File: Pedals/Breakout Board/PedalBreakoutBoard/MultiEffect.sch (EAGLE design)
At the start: 69 parts, among them IC1 LD1117V, IC2 MCP6004P, U1 OPA1652AID

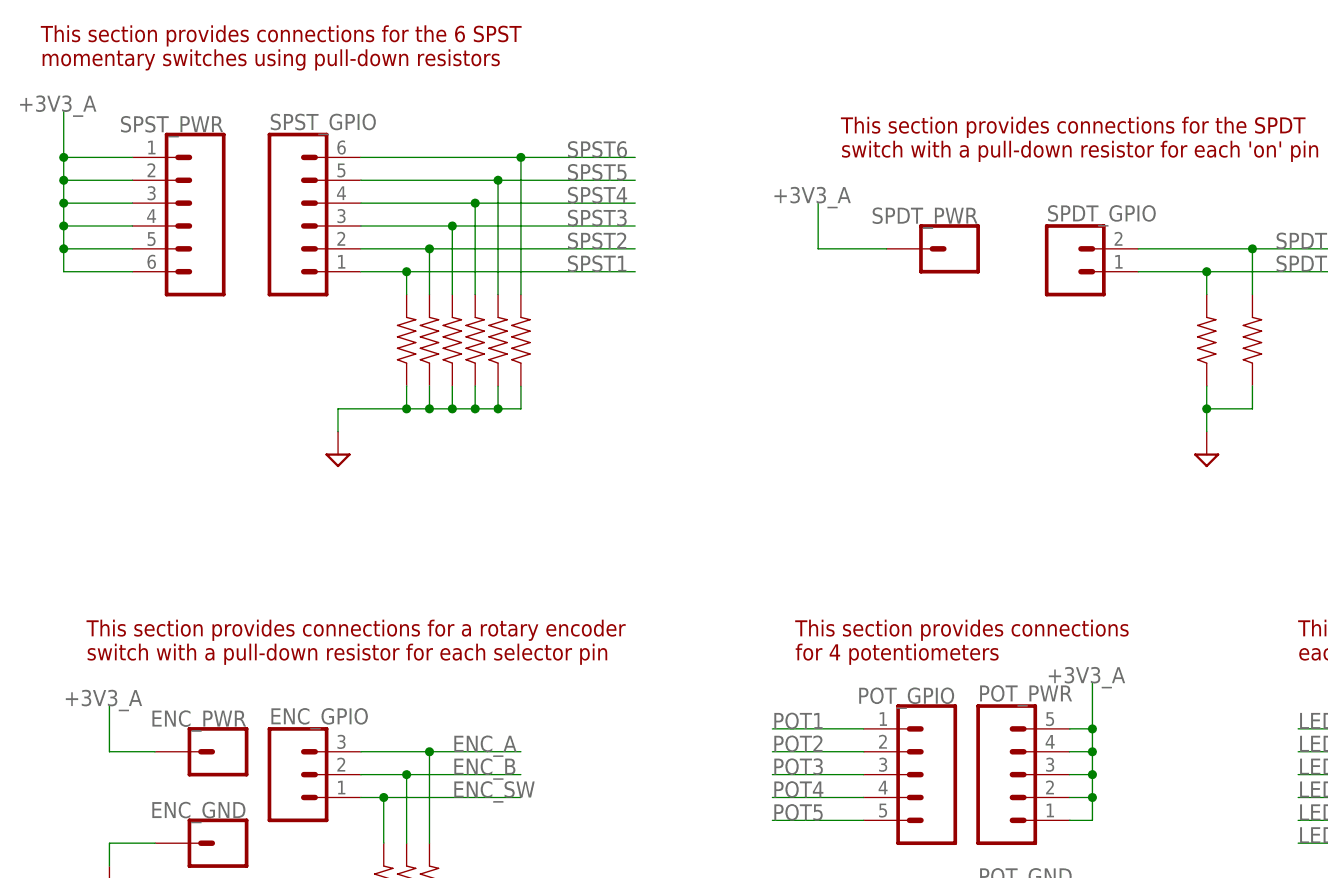
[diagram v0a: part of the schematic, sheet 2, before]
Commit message: DP-97 - Finish updating grounding scheme on multi-effect pedal
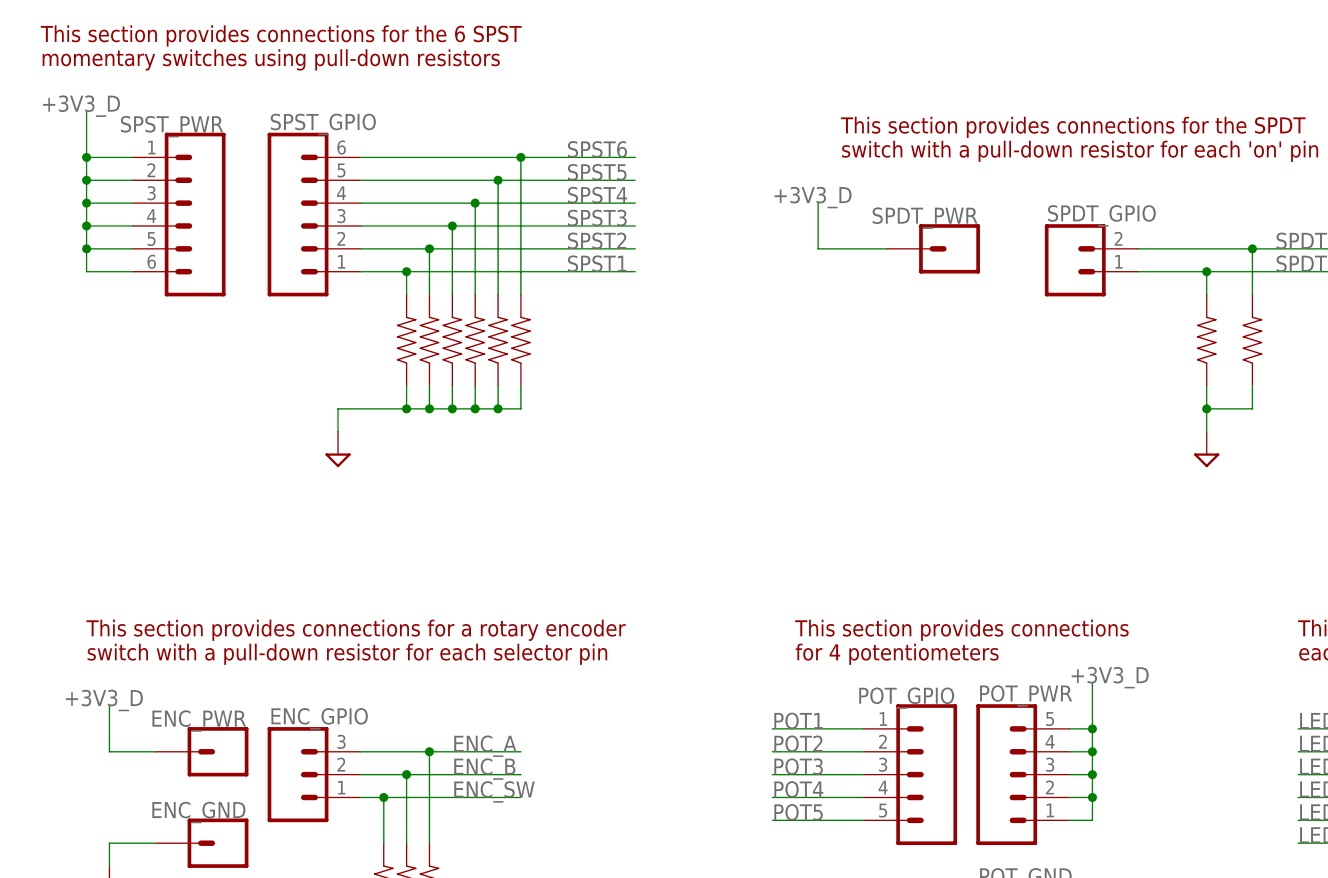
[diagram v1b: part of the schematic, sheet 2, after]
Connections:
- net +3V3_A: no longer ENC_PWR.1, POT_PWR.1, POT_PWR.2, POT_PWR.3, POT_PWR.4, POT_PWR.5, SPDT_PWR.1, SPST_PWR.1, SPST_PWR.2, SPST_PWR.3, SPST_PWR.4, SPST_PWR.5, SPST_PWR.6
- net +3V3_D: now also ENC_PWR.1, POT_PWR.1, POT_PWR.2, POT_PWR.3, POT_PWR.4, POT_PWR.5, SPDT_PWR.1, SPST_PWR.1, SPST_PWR.2, SPST_PWR.3, SPST_PWR.4, SPST_PWR.5, SPST_PWR.6
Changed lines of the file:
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@@
 <attribute name="VALUE" x="129.54" y="60.96" size="1.778" layer="94" rot="R180"/>
 </instance>
-<instance part="SUPPLY2" gate="GND" x="142.24" y="119.38" smashed="yes" rot="R90">
-<attribute name="VALUE" x="145.415" y="117.475" size="1.778" layer="96" rot="R90"/>
+<instance part="SUPPLY2" gate="GND" x="157.48" y="111.76" smashed="yes">
+<attribute name="VALUE" x="155.575" y="108.585" size="1.778" layer="96"/>
 </instance>
 <instance part="SUPPLY9" gate="GND" x="22.86" y="0" smashed="yes" grouprefs="POWER">
@@
 <pinref part="SEED" gate="G$1" pin="GND"/>
 <pinref part="SUPPLY2" gate="GND" pin="GND"/>
-<wire x1="134.62" y1="114.3" x2="139.7" y2="114.3" width="0.1524" layer="91"/>
-<wire x1="139.7" y1="114.3" x2="139.7" y2="119.38" width="0.1524" layer="91"/>
+<wire x1="134.62" y1="114.3" x2="157.48" y2="114.3" width="0.1524" layer="91"/>
 </segment>
 <segment>
@@
 <net name="+3V3_A" class="0">
 <segment>
-<wire x1="68.58" y1="-12.7" x2="71.12" y2="-12.7" width="0.1524" layer="91" grouprefs="POT"/>
-<wire x1="71.12" y1="-12.7" x2="71.12" y2="-10.16" width="0.1524" layer="91" grouprefs="POT"/>
-<wire x1="71.12" y1="-10.16" x2="71.12" y2="-7.62" width="0.1524" layer="91" grouprefs="POT"/>
-<wire x1="71.12" y1="-7.62" x2="71.12" y2="-5.08" width="0.1524" layer="91" grouprefs="POT"/>
-<wire x1="71.12" y1="-5.08" x2="71.12" y2="-2.54" width="0.1524" layer="91" grouprefs="POT"/>
-<wire x1="71.12" y1="-2.54" x2="71.12" y2="2.54" width="0.1524" layer="91" grouprefs="POT"/>
-<wire x1="68.58" y1="-10.16" x2="71.12" y2="-10.16" width="0.1524" layer="91" grouprefs="POT"/>
-<junction x="71.12" y="-10.16" grouprefs="POT"/>
-<wire x1="68.58" y1="-7.62" x2="71.12" y2="-7.62" width="0.1524" layer="91" grouprefs="POT"/>
-<junction x="71.12" y="-7.62" grouprefs="POT"/>
-<wire x1="68.58" y1="-5.08" x2="71.12" y2="-5.08" width="0.1524" layer="91" grouprefs="POT"/>
-<junction x="71.12" y="-5.08" grouprefs="POT"/>
-<label x="66.04" y="2.54" size="1.778" layer="95" grouprefs="POT"/>
-<pinref part="POT_PWR" gate="G$1" pin="1"/>
-<pinref part="POT_PWR" gate="G$1" pin="2"/>
-<pinref part="POT_PWR" gate="G$1" pin="3"/>
-<pinref part="POT_PWR" gate="G$1" pin="4"/>
-<pinref part="POT_PWR" gate="G$1" pin="5"/>
-<wire x1="68.58" y1="-2.54" x2="71.12" y2="-2.54" width="0.1524" layer="91" grouprefs="POT"/>
-<junction x="71.12" y="-2.54"/>
-</segment>
-<segment>
-<wire x1="-43.18" y1="60.96" x2="-43.18" y2="66.04" width="0.1524" layer="91" grouprefs="SPST"/>
-<wire x1="-35.56" y1="60.96" x2="-43.18" y2="60.96" width="0.1524" layer="91" grouprefs="SPST"/>
-<label x="-48.26" y="66.04" size="1.778" layer="95" grouprefs="SPST"/>
-<pinref part="SPST_PWR" gate="G$1" pin="1"/>
-<pinref part="SPST_PWR" gate="G$1" pin="6"/>
-<wire x1="-35.56" y1="48.26" x2="-43.18" y2="48.26" width="0.1524" layer="91" grouprefs="SPST"/>
-<wire x1="-43.18" y1="48.26" x2="-43.18" y2="50.8" width="0.1524" layer="91" grouprefs="SPST"/>
-<junction x="-43.18" y="60.96" grouprefs="SPST"/>
-<pinref part="SPST_PWR" gate="G$1" pin="2"/>
-<wire x1="-43.18" y1="50.8" x2="-43.18" y2="53.34" width="0.1524" layer="91" grouprefs="SPST"/>
-<wire x1="-43.18" y1="53.34" x2="-43.18" y2="55.88" width="0.1524" layer="91" grouprefs="SPST"/>
-<wire x1="-43.18" y1="55.88" x2="-43.18" y2="58.42" width="0.1524" layer="91" grouprefs="SPST"/>
-<wire x1="-43.18" y1="58.42" x2="-43.18" y2="60.96" width="0.1524" layer="91" grouprefs="SPST"/>
-<wire x1="-35.56" y1="58.42" x2="-43.18" y2="58.42" width="0.1524" layer="91" grouprefs="SPST"/>
-<junction x="-43.18" y="58.42" grouprefs="SPST"/>
-<pinref part="SPST_PWR" gate="G$1" pin="3"/>
-<wire x1="-35.56" y1="55.88" x2="-43.18" y2="55.88" width="0.1524" layer="91" grouprefs="SPST"/>
-<junction x="-43.18" y="55.88" grouprefs="SPST"/>
-<pinref part="SPST_PWR" gate="G$1" pin="4"/>
-<wire x1="-35.56" y1="53.34" x2="-43.18" y2="53.34" width="0.1524" layer="91" grouprefs="SPST"/>
-<junction x="-43.18" y="53.34" grouprefs="SPST"/>
-<pinref part="SPST_PWR" gate="G$1" pin="5"/>
-<wire x1="-35.56" y1="50.8" x2="-43.18" y2="50.8" width="0.1524" layer="91" grouprefs="SPST"/>
-<junction x="-43.18" y="50.8" grouprefs="SPST"/>
-</segment>
-<segment>
-<wire x1="40.64" y1="50.8" x2="40.64" y2="55.88" width="0.1524" layer="91" grouprefs="SPDT"/>
-<wire x1="48.26" y1="50.8" x2="40.64" y2="50.8" width="0.1524" layer="91" grouprefs="SPDT"/>
-<label x="35.56" y="55.88" size="1.778" layer="95" grouprefs="SPDT"/>
-<pinref part="SPDT_PWR" gate="G$1" pin="1"/>
-</segment>
-<segment>
-<pinref part="ENC_PWR" gate="G$1" pin="1"/>
-<wire x1="-33.02" y1="-5.08" x2="-38.1" y2="-5.08" width="0.1524" layer="91" grouprefs="ENCODER"/>
-<wire x1="-38.1" y1="-5.08" x2="-38.1" y2="0" width="0.1524" layer="91" grouprefs="ENCODER"/>
-<label x="-43.18" y="0" size="1.778" layer="95" grouprefs="ENCODER"/>
-</segment>
-<segment>
 <pinref part="EXT_PWR_A" gate="G$1" pin="1"/>
 <wire x1="198.12" y1="0" x2="205.74" y2="0" width="0.1524" layer="91" grouprefs="EXTRA"/>
@@
 <label x="160.02" y="10.16" size="1.778" layer="95" grouprefs="EXTRA"/>
 </segment>
-</net>
+<segment>
+<pinref part="SPST_PWR" gate="G$1" pin="1"/>
+<wire x1="-35.56" y1="60.96" x2="-40.64" y2="60.96" width="0.1524" layer="91" grouprefs="SPST"/>
+<wire x1="-40.64" y1="60.96" x2="-40.64" y2="66.04" width="0.1524" layer="91" grouprefs="SPST"/>
+<wire x1="-40.64" y1="60.96" x2="-40.64" y2="58.42" width="0.1524" layer="91" grouprefs="SPST"/>
+<junction x="-40.64" y="60.96" grouprefs="SPST"/>
+<pinref part="SPST_PWR" gate="G$1" pin="6"/>
+<wire x1="-40.64" y1="58.42" x2="-40.64" y2="55.88" width="0.1524" layer="91" grouprefs="SPST"/>
+<wire x1="-40.64" y1="55.88" x2="-40.64" y2="53.34" width="0.1524" layer="91" grouprefs="SPST"/>
+<wire x1="-40.64" y1="53.34" x2="-40.64" y2="50.8" width="0.1524" layer="91" grouprefs="SPST"/>
+<wire x1="-40.64" y1="50.8" x2="-40.64" y2="48.26" width="0.1524" layer="91" grouprefs="SPST"/>
+<wire x1="-40.64" y1="48.26" x2="-35.56" y2="48.26" width="0.1524" layer="91" grouprefs="SPST"/>
+<pinref part="SPST_PWR" gate="G$1" pin="5"/>
+<wire x1="-35.56" y1="50.8" x2="-40.64" y2="50.8" width="0.1524" layer="91" grouprefs="SPST"/>
+<junction x="-40.64" y="50.8" grouprefs="SPST"/>
+<pinref part="SPST_PWR" gate="G$1" pin="4"/>
+<wire x1="-35.56" y1="53.34" x2="-40.64" y2="53.34" width="0.1524" layer="91" grouprefs="SPST"/>
+<junction x="-40.64" y="53.34" grouprefs="SPST"/>
+<pinref part="SPST_PWR" gate="G$1" pin="3"/>
+<wire x1="-35.56" y1="55.88" x2="-40.64" y2="55.88" width="0.1524" layer="91" grouprefs="SPST"/>
+<junction x="-40.64" y="55.88" grouprefs="SPST"/>
+<pinref part="SPST_PWR" gate="G$1" pin="2"/>
+<wire x1="-35.56" y1="58.42" x2="-40.64" y2="58.42" width="0.1524" layer="91" grouprefs="SPST"/>
+<junction x="-40.64" y="58.42" grouprefs="SPST"/>
+<label x="-45.72" y="66.04" size="1.778" layer="95"/>
+</segment>
+<segment>
+<pinref part="SPDT_PWR" gate="G$1" pin="1"/>
+<wire x1="48.26" y1="50.8" x2="40.64" y2="50.8" width="0.1524" layer="91" grouprefs="SPDT"/>
+<wire x1="40.64" y1="50.8" x2="40.64" y2="55.88" width="0.1524" layer="91" grouprefs="SPDT"/>
+<label x="35.56" y="55.88" size="1.778" layer="95" grouprefs="SPDT"/>
+</segment>
+<segment>
+<pinref part="POT_PWR" gate="G$1" pin="1"/>
+<wire x1="68.58" y1="-12.7" x2="71.12" y2="-12.7" width="0.1524" layer="91"/>
+<wire x1="71.12" y1="-12.7" x2="71.12" y2="-10.16" width="0.1524" layer="91"/>
+<pinref part="POT_PWR" gate="G$1" pin="2"/>
+<wire x1="71.12" y1="-10.16" x2="71.12" y2="-7.62" width="0.1524" layer="91"/>
+<wire x1="71.12" y1="-7.62" x2="71.12" y2="-5.08" width="0.1524" layer="91"/>
+<wire x1="71.12" y1="-5.08" x2="71.12" y2="-2.54" width="0.1524" layer="91"/>
+<wire x1="71.12" y1="-2.54" x2="71.12" y2="2.54" width="0.1524" layer="91" grouprefs="POT"/>
+<wire x1="68.58" y1="-10.16" x2="71.12" y2="-10.16" width="0.1524" layer="91"/>
+<junction x="71.12" y="-10.16"/>
+<pinref part="POT_PWR" gate="G$1" pin="3"/>
+<wire x1="68.58" y1="-7.62" x2="71.12" y2="-7.62" width="0.1524" layer="91"/>
+<junction x="71.12" y="-7.62"/>
+<pinref part="POT_PWR" gate="G$1" pin="4"/>
+<wire x1="68.58" y1="-5.08" x2="71.12" y2="-5.08" width="0.1524" layer="91"/>
+<junction x="71.12" y="-5.08"/>
+<pinref part="POT_PWR" gate="G$1" pin="5"/>
+<wire x1="68.58" y1="-2.54" x2="71.12" y2="-2.54" width="0.1524" layer="91"/>
+<junction x="71.12" y="-2.54"/>
+<label x="68.58" y="2.54" size="1.778" layer="95" grouprefs="POT"/>
+</segment>
+<segment>
+<pinref part="ENC_PWR" gate="G$1" pin="1"/>
+<wire x1="-33.02" y1="-5.08" x2="-38.1" y2="-5.08" width="0.1524" layer="91"/>
+<wire x1="-38.1" y1="-5.08" x2="-38.1" y2="0" width="0.1524" layer="91" grouprefs="ENCODER"/>
+<label x="-43.18" y="0" size="1.778" layer="95" grouprefs="ENCODER"/>
+</segment>
+</net>
